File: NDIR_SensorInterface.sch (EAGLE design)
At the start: 2 parts, among them J1 CONN_I2C_SENSOR_BOARD_MOUNT_T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, J2 CONN_42.54

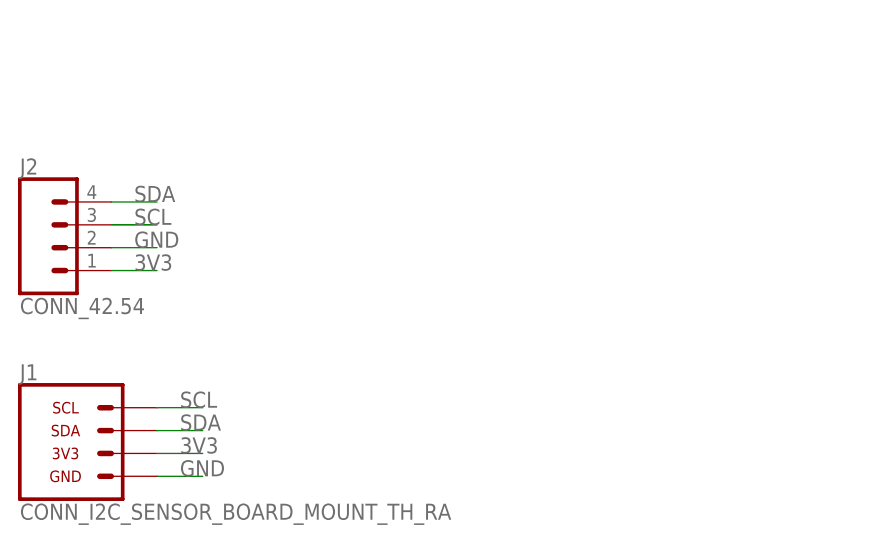
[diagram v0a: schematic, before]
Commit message: Updated NDIR interface board to v1.0
Added reverse polarity protection and I2C pull up resistors
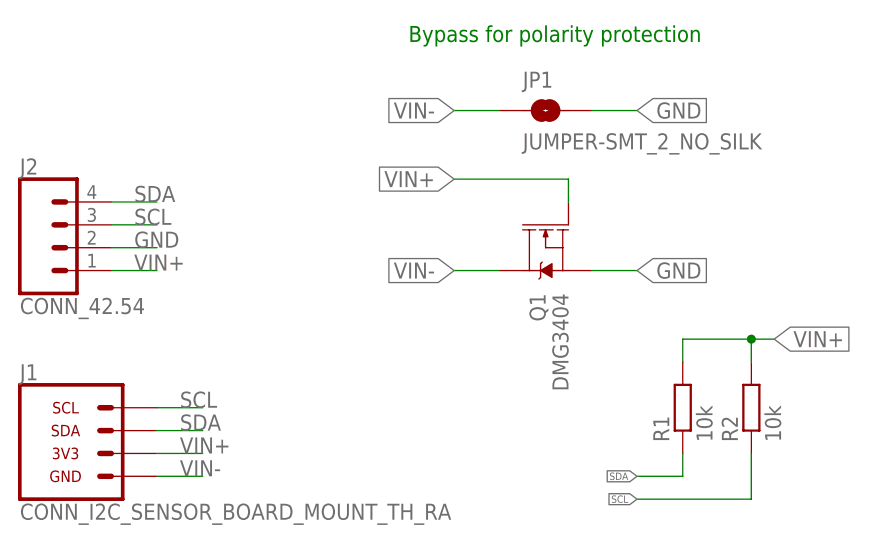
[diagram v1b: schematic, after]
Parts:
- added JP1: JUMPER-SMT_2_NO_SILK, bschulz:JUMPER-SMT_2_NO_SILK
- added Q1: DMG3404, bschulz:MOSFET-NCH-DMG3404L
- added R1, R2: 10k, bschulz_passives:R-EU_10KR0603
- J2: DIGIKEY (none) -> ED7564-04-ND; MF (none) -> Mill-Max; MPN (none) -> 800-10-004-10-002000
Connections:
- removed net 3V3: J1.2, J2.1
- new net VIN+: J1.3V3, J2.1, Q1.G, R1.2, R2.2
- new net VIN-: J1.GND, JP1.1, Q1.D
- net GND: now also JP1.2, Q1.S; no longer J1.1
- net SCL: now also J1.SCL, R2.1; no longer J1.4
- net SDA: now also J1.SDA, R1.1; no longer J1.3
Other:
- note added: "Bypass for polarity protection"
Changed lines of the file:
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@@
 <parts>
 <part name="J1" library="GEMS_Plugs" deviceset="CONN_I2C_SENSOR" device="_BOARD_MOUNT_TH_RA"/>
-<part name="J2" library="bschulz" deviceset="CONN_4" device="2.54"/>
+<part name="J2" library="bschulz" deviceset="CONN_4" device="2.54">
+<attribute name="DIGIKEY" value="ED7564-04-ND"/>
+<attribute name="MF" value="Mill-Max"/>
+<attribute name="MPN" value="800-10-004-10-002000"/>
+</part>
+<part name="Q1" library="bschulz" deviceset="MOSFET-NCH" device="-DMG3404L" value="DMG3404"/>
+<part name="JP1" library="bschulz" deviceset="JUMPER-SMT_2_NO" device="_SILK" package3d_urn="urn:adsk.eagle:package:39279/1"/>
+<part name="R1" library="bschulz_passives" deviceset="R-EU_" device="R0603" technology="10K" value="10k"/>
+<part name="R2" library="bschulz_passives" deviceset="R-EU_" device="R0603" technology="10K" value="10k"/>
 </parts>
 <sheets>
 <sheet>
 <plain>
+<text x="60.96" y="81.28" size="1.778" layer="91">Bypass for polarity protection</text>
 </plain>
 <instances>
@@
 <attribute name="VALUE" x="17.78" y="51.054" size="1.778" layer="96" font="vector"/>
 <attribute name="NAME" x="17.78" y="66.548" size="1.778" layer="95" font="vector"/>
+<attribute name="DIGIKEY" x="22.86" y="58.42" size="1.778" layer="96" display="off"/>
+<attribute name="MF" x="22.86" y="58.42" size="1.778" layer="96" display="off"/>
+<attribute name="MPN" x="22.86" y="58.42" size="1.778" layer="96" display="off"/>
+</instance>
+<instance part="Q1" gate="NMOS" x="76.2" y="58.42" smashed="yes" rot="MR270">
+<attribute name="NAME" x="76.2" y="53.34" size="1.778" layer="95" font="vector" rot="MR270"/>
+<attribute name="VALUE" x="78.74" y="53.34" size="1.778" layer="96" font="vector" rot="MR270"/>
+</instance>
+<instance part="JP1" gate="G$1" x="76.2" y="73.66" smashed="yes">
+<attribute name="NAME" x="73.66" y="76.2" size="1.778" layer="95" font="vector"/>
+<attribute name="VALUE" x="73.66" y="71.12" size="1.778" layer="96" font="vector" align="top-left"/>
+</instance>
+<instance part="R1" gate="G$1" x="91.44" y="40.64" smashed="yes" rot="R90">
+<attribute name="NAME" x="89.9414" y="36.83" size="1.778" layer="95" rot="R90"/>
+<attribute name="VALUE" x="94.742" y="36.83" size="1.778" layer="96" rot="R90"/>
+</instance>
+<instance part="R2" gate="G$1" x="99.06" y="40.64" smashed="yes" rot="R90">
+<attribute name="NAME" x="97.5614" y="36.83" size="1.778" layer="95" rot="R90"/>
+<attribute name="VALUE" x="102.362" y="36.83" size="1.778" layer="96" rot="R90"/>
 </instance>
 </instances>
@@
 </busses>
 <nets>
-<net name="3V3" class="0">
+<net name="GND" class="0">
 <segment>
-<pinref part="J2" gate="G$1" pin="1"/>
-<wire x1="27.94" y1="55.88" x2="33.02" y2="55.88" width="0.1524" layer="91"/>
-<label x="30.48" y="55.88" size="1.778" layer="95"/>
+<pinref part="Q1" gate="NMOS" pin="S"/>
+<wire x1="81.28" y1="55.88" x2="86.36" y2="55.88" width="0.1524" layer="91"/>
+<label x="86.36" y="55.88" size="1.778" layer="95" xref="yes"/>
 </segment>
-<segment>
-<pinref part="J1" gate="G$1" pin="2"/>
-<wire x1="33.02" y1="35.56" x2="38.1" y2="35.56" width="0.1524" layer="91"/>
-<label x="35.56" y="35.56" size="1.778" layer="95"/>
-</segment>
-</net>
-<net name="GND" class="0">
 <segment>
 <pinref part="J2" gate="G$1" pin="2"/>
@@
 </segment>
 <segment>
-<pinref part="J1" gate="G$1" pin="1"/>
-<wire x1="33.02" y1="33.02" x2="38.1" y2="33.02" width="0.1524" layer="91"/>
-<label x="35.56" y="33.02" size="1.778" layer="95"/>
+<pinref part="JP1" gate="G$1" pin="2"/>
+<wire x1="81.28" y1="73.66" x2="86.36" y2="73.66" width="0.1524" layer="91"/>
+<label x="86.36" y="73.66" size="1.778" layer="95" xref="yes"/>
 </segment>
 </net>
@@
 </segment>
 <segment>
-<pinref part="J1" gate="G$1" pin="4"/>
+<pinref part="J1" gate="G$1" pin="SCL"/>
 <wire x1="33.02" y1="40.64" x2="38.1" y2="40.64" width="0.1524" layer="91"/>
 <label x="35.56" y="40.64" size="1.778" layer="95"/>
 </segment>
+<segment>
+<pinref part="R2" gate="G$1" pin="1"/>
+<wire x1="99.06" y1="35.56" x2="99.06" y2="30.48" width="0.1524" layer="91"/>
+<wire x1="99.06" y1="30.48" x2="86.36" y2="30.48" width="0.1524" layer="91"/>
+<label x="86.36" y="30.48" size="0.8128" layer="95" rot="R180" xref="yes"/>
+</segment>
 </net>
 <net name="SDA" class="0">
+<segment>
+<pinref part="J1" gate="G$1" pin="SDA"/>
+<wire x1="33.02" y1="38.1" x2="38.1" y2="38.1" width="0.1524" layer="91"/>
+<label x="35.56" y="38.1" size="1.778" layer="95"/>
+</segment>
 <segment>
 <pinref part="J2" gate="G$1" pin="4"/>
@@
 </segment>
 <segment>
-<pinref part="J1" gate="G$1" pin="3"/>
-<wire x1="33.02" y1="38.1" x2="38.1" y2="38.1" width="0.1524" layer="91"/>
-<label x="35.56" y="38.1" size="1.778" layer="95"/>
+<pinref part="R1" gate="G$1" pin="1"/>
+<wire x1="91.44" y1="35.56" x2="91.44" y2="33.02" width="0.1524" layer="91"/>
+<wire x1="91.44" y1="33.02" x2="86.36" y2="33.02" width="0.1524" layer="91"/>
+<label x="86.36" y="33.02" size="0.8128" layer="95" rot="R180" xref="yes"/>
+</segment>
+</net>
+<net name="VIN-" class="0">
+<segment>
+<pinref part="Q1" gate="NMOS" pin="D"/>
+<wire x1="71.12" y1="55.88" x2="66.04" y2="55.88" width="0.1524" layer="91"/>
+<label x="66.04" y="55.88" size="1.778" layer="95" rot="R180" xref="yes"/>
+</segment>
+<segment>
+<pinref part="J1" gate="G$1" pin="GND"/>
+<wire x1="33.02" y1="33.02" x2="38.1" y2="33.02" width="0.1524" layer="91"/>
+<label x="35.56" y="33.02" size="1.778" layer="95"/>
+</segment>
+<segment>
+<pinref part="JP1" gate="G$1" pin="1"/>
+<wire x1="71.12" y1="73.66" x2="66.04" y2="73.66" width="0.1524" layer="91"/>
+<label x="66.04" y="73.66" size="1.778" layer="95" rot="R180" xref="yes"/>
+</segment>
+</net>
+<net name="VIN+" class="0">
+<segment>
+<pinref part="Q1" gate="NMOS" pin="G"/>
+<wire x1="78.74" y1="63.5" x2="78.74" y2="66.04" width="0.1524" layer="91"/>
+<wire x1="78.74" y1="66.04" x2="66.04" y2="66.04" width="0.1524" layer="91"/>
+<label x="66.04" y="66.04" size="1.778" layer="95" rot="R180" xref="yes"/>
+</segment>
+<segment>
+<pinref part="J1" gate="G$1" pin="3V3"/>
+<wire x1="33.02" y1="35.56" x2="38.1" y2="35.56" width="0.1524" layer="91"/>
+<label x="35.56" y="35.56" size="1.778" layer="95"/>
+</segment>
+<segment>
+<pinref part="J2" gate="G$1" pin="1"/>
+<wire x1="27.94" y1="55.88" x2="33.02" y2="55.88" width="0.1524" layer="91"/>
+<label x="30.48" y="55.88" size="1.778" layer="95"/>
+</segment>
+<segment>
+<pinref part="R1" gate="G$1" pin="2"/>
+<wire x1="91.44" y1="45.72" x2="91.44" y2="48.26" width="0.1524" layer="91"/>
+<wire x1="91.44" y1="48.26" x2="99.06" y2="48.26" width="0.1524" layer="91"/>
+<pinref part="R2" gate="G$1" pin="2"/>
+<wire x1="99.06" y1="48.26" x2="99.06" y2="45.72" width="0.1524" layer="91"/>
+<wire x1="99.06" y1="48.26" x2="101.6" y2="48.26" width="0.1524" layer="91"/>
+<junction x="99.06" y="48.26"/>
+<label x="101.6" y="48.26" size="1.778" layer="95" xref="yes"/>
 </segment>
 </net>
@@
 </schematic>
 </drawing>
+<compatibility>
+<note version="8.3" severity="warning">
+Since Version 8.3, EAGLE supports URNs for individual library
+assets (packages, symbols, and devices). The URNs of those assets
+will not be understood (or retained) with this version.
+</note>
+<note version="8.3" severity="warning">
+Since Version 8.3, EAGLE supports the association of 3D packages
+with devices in libraries, schematics, and board files. Those 3D
+packages will not be understood (or retained) with this version.
+</note>
+</compatibility>
 </eagle>
